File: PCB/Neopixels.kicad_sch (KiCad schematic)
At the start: 47 parts

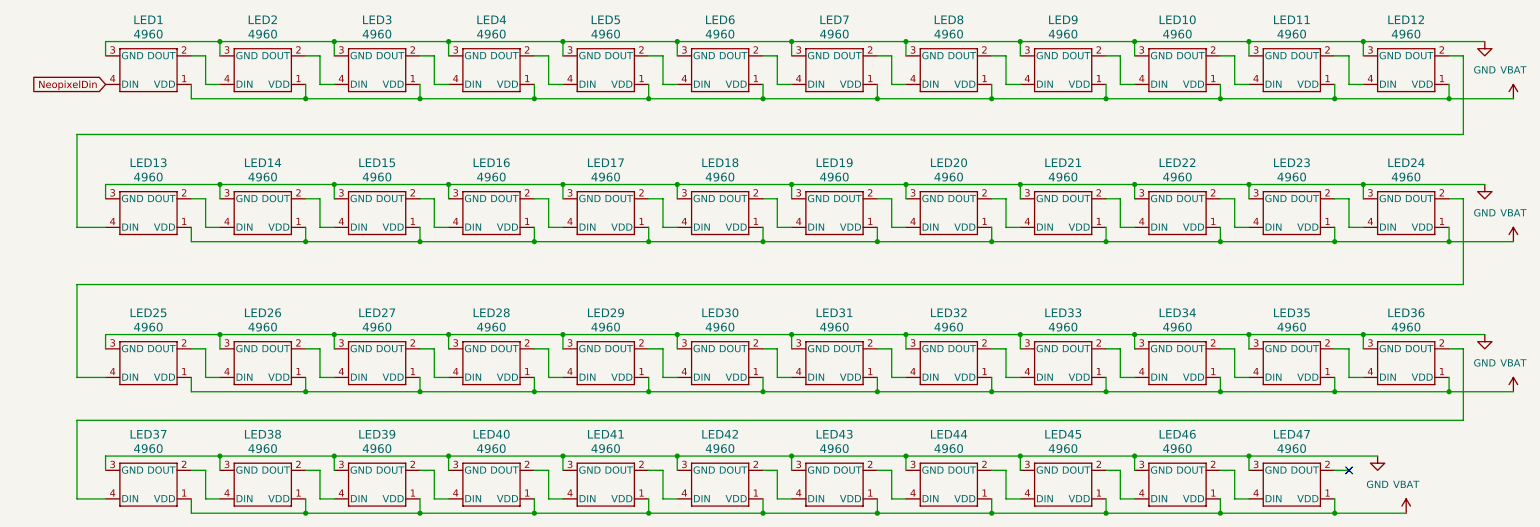
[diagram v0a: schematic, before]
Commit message: reorg symbols to be locally stored
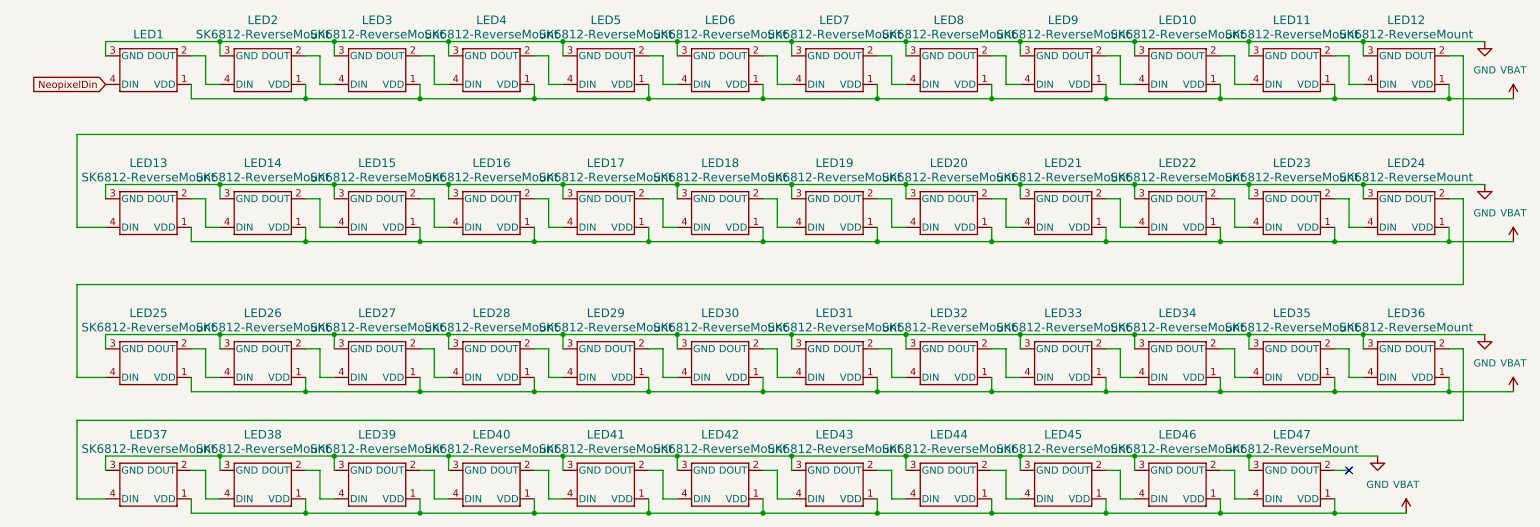
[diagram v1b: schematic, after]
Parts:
- LED1, LED10, LED11, LED12, LED13, LED14, LED15, LED16, LED17, LED18, LED19, LED2, LED20, LED21, LED22, LED23, LED24, LED25, LED26, LED27, LED28, LED29, LED3, LED30, LED31, LED32, LED33, LED34, LED35, LED36, LED37, LED38, LED39, LED4, LED40, LED41, LED42, LED43, LED44, LED45, LED46, LED47, LED5, LED6, LED7, LED8, LED9: value 4960 -> SK6812-ReverseMount; footprint kbd:YS-SK6812MINI-E -> 4960_ADA; symbol SK6812 Reverse mount:4960 -> Local-lib:SK6812-ReverseMount

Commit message: update to use local footprints
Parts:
- LED1, LED10, LED11, LED12, LED13, LED14, LED15, LED16, LED17, LED18, LED19, LED2, LED20, LED21, LED22, LED23, LED24, LED25, LED26, LED27, LED28, LED29, LED3, LED30, LED31, LED32, LED33, LED34, LED35, LED36, LED37, LED38, LED39, LED4, LED40, LED41, LED42, LED43, LED44, LED45, LED46, LED47, LED5, LED6, LED7, LED8, LED9: footprint 4960_ADA -> Local-lib:YS-SK6812MINI-E
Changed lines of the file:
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@@
 			)
 		)
-		(property "Footprint" "4960_ADA"
+		(property "Footprint" "Local-lib:YS-SK6812MINI-E"
 			(at 76.2 82.55 0)
 			(hide yes)
@@
 			)
 		)
-		(property "Footprint" "4960_ADA"
+		(property "Footprint" "Local-lib:YS-SK6812MINI-E"
 			(at 55.88 55.88 0)
 			(hide yes)
@@
 			)
 		)
-		(property "Footprint" "4960_ADA"
+		(property "Footprint" "Local-lib:YS-SK6812MINI-E"
 			(at 177.8 55.88 0)
 			(hide yes)
@@
 			)
 		)
-		(property "Footprint" "4960_ADA"
+		(property "Footprint" "Local-lib:YS-SK6812MINI-E"
 			(at 116.84 104.14 0)
 			(hide yes)
@@
 			)
 		)
-		(property "Footprint" "4960_ADA"
+		(property "Footprint" "Local-lib:YS-SK6812MINI-E"
 			(at 177.8 30.48 0)
 			(hide yes)
@@
 			)
 		)
-		(property "Footprint" "4960_ADA"
+		(property "Footprint" "Local-lib:YS-SK6812MINI-E"
 			(at 157.48 30.48 0)
 			(hide yes)
@@
 			)
 		)
-		(property "Footprint" "4960_ADA"
+		(property "Footprint" "Local-lib:YS-SK6812MINI-E"
 			(at 177.8 104.14 0)
 			(hide yes)
@@
 			)
 		)
-		(property "Footprint" "4960_ADA"
+		(property "Footprint" "Local-lib:YS-SK6812MINI-E"
 			(at 137.16 82.55 0)
 			(hide yes)
@@
 			)
 		)
-		(property "Footprint" "4960_ADA"
+		(property "Footprint" "Local-lib:YS-SK6812MINI-E"
 			(at 96.52 82.55 0)
 			(hide yes)
@@
 			)
 		)
-		(property "Footprint" "4960_ADA"
+		(property "Footprint" "Local-lib:YS-SK6812MINI-E"
 			(at 137.16 30.48 0)
 			(hide yes)
@@
 			)
 		)
-		(property "Footprint" "4960_ADA"
+		(property "Footprint" "Local-lib:YS-SK6812MINI-E"
 			(at 259.08 30.48 0)
 			(hide yes)
@@
 			)
 		)
-		(property "Footprint" "4960_ADA"
+		(property "Footprint" "Local-lib:YS-SK6812MINI-E"
 			(at 35.56 82.55 0)
 			(hide yes)
@@
 			)
 		)
-		(property "Footprint" "4960_ADA"
+		(property "Footprint" "Local-lib:YS-SK6812MINI-E"
 			(at 137.16 104.14 0)
 			(hide yes)
@@
 			)
 		)
-		(property "Footprint" "4960_ADA"
+		(property "Footprint" "Local-lib:YS-SK6812MINI-E"
 			(at 198.12 55.88 0)
 			(hide yes)
@@
 			)
 		)
-		(property "Footprint" "4960_ADA"
+		(property "Footprint" "Local-lib:YS-SK6812MINI-E"
 			(at 218.44 30.48 0)
 			(hide yes)
@@
 			)
 		)
-		(property "Footprint" "4960_ADA"
+		(property "Footprint" "Local-lib:YS-SK6812MINI-E"
 			(at 116.84 30.48 0)
 			(hide yes)
@@
 			)
 		)
-		(property "Footprint" "4960_ADA"
+		(property "Footprint" "Local-lib:YS-SK6812MINI-E"
 			(at 157.48 55.88 0)
 			(hide yes)
@@
 			)
 		)
-		(property "Footprint" "4960_ADA"
+		(property "Footprint" "Local-lib:YS-SK6812MINI-E"
 			(at 177.8 82.55 0)
 			(hide yes)
@@
 			)
 		)
-		(property "Footprint" "4960_ADA"
+		(property "Footprint" "Local-lib:YS-SK6812MINI-E"
 			(at 76.2 30.48 0)
 			(hide yes)
@@
 			)
 		)
-		(property "Footprint" "4960_ADA"
+		(property "Footprint" "Local-lib:YS-SK6812MINI-E"
 			(at 35.56 104.14 0)
 			(hide yes)
@@
 			)
 		)
-		(property "Footprint" "4960_ADA"
+		(property "Footprint" "Local-lib:YS-SK6812MINI-E"
 			(at 55.88 104.14 0)
 			(hide yes)
@@
 			)
 		)
-		(property "Footprint" "4960_ADA"
+		(property "Footprint" "Local-lib:YS-SK6812MINI-E"
 			(at 116.84 82.55 0)
 			(hide yes)
@@
 			)
 		)
-		(property "Footprint" "4960_ADA"
+		(property "Footprint" "Local-lib:YS-SK6812MINI-E"
 			(at 198.12 30.48 0)
 			(hide yes)
@@
 			)
 		)
-		(property "Footprint" "4960_ADA"
+		(property "Footprint" "Local-lib:YS-SK6812MINI-E"
 			(at 198.12 104.14 0)
 			(hide yes)
@@
 			)
 		)
-		(property "Footprint" "4960_ADA"
+		(property "Footprint" "Local-lib:YS-SK6812MINI-E"
 			(at 35.56 30.48 0)
 			(hide yes)
@@
 			)
 		)
-		(property "Footprint" "4960_ADA"
+		(property "Footprint" "Local-lib:YS-SK6812MINI-E"
 			(at 96.52 55.88 0)
 			(hide yes)
@@
 			)
 		)
-		(property "Footprint" "4960_ADA"
+		(property "Footprint" "Local-lib:YS-SK6812MINI-E"
 			(at 55.88 30.48 0)
 			(hide yes)
@@
 			)
 		)
-		(property "Footprint" "4960_ADA"
+		(property "Footprint" "Local-lib:YS-SK6812MINI-E"
 			(at 76.2 55.88 0)
 			(hide yes)
@@
 			)
 		)
-		(property "Footprint" "4960_ADA"
+		(property "Footprint" "Local-lib:YS-SK6812MINI-E"
 			(at 55.88 82.55 0)
 			(hide yes)
@@
 			)
 		)
-		(property "Footprint" "4960_ADA"
+		(property "Footprint" "Local-lib:YS-SK6812MINI-E"
 			(at 35.56 55.88 0)
 			(hide yes)
@@
 			)
 		)
-		(property "Footprint" "4960_ADA"
+		(property "Footprint" "Local-lib:YS-SK6812MINI-E"
 			(at 218.44 104.14 0)
 			(hide yes)
@@
 			)
 		)
-		(property "Footprint" "4960_ADA"
+		(property "Footprint" "Local-lib:YS-SK6812MINI-E"
 			(at 259.08 82.55 0)
 			(hide yes)
@@
 			)
 		)
-		(property "Footprint" "4960_ADA"
+		(property "Footprint" "Local-lib:YS-SK6812MINI-E"
 			(at 137.16 55.88 0)
 			(hide yes)
@@
 			)
 		)
-		(property "Footprint" "4960_ADA"
+		(property "Footprint" "Local-lib:YS-SK6812MINI-E"
 			(at 218.44 82.55 0)
 			(hide yes)
@@
 			)
 		)
-		(property "Footprint" "4960_ADA"
+		(property "Footprint" "Local-lib:YS-SK6812MINI-E"
 			(at 218.44 55.88 0)
 			(hide yes)
@@
 			)
 		)
-		(property "Footprint" "4960_ADA"
+		(property "Footprint" "Local-lib:YS-SK6812MINI-E"
 			(at 238.76 104.14 0)
 			(hide yes)
@@
 			)
 		)
-		(property "Footprint" "4960_ADA"
+		(property "Footprint" "Local-lib:YS-SK6812MINI-E"
 			(at 96.52 104.14 0)
 			(hide yes)
@@
 			)
 		)
-		(property "Footprint" "4960_ADA"
+		(property "Footprint" "Local-lib:YS-SK6812MINI-E"
 			(at 259.08 55.88 0)
 			(hide yes)
@@
 			)
 		)
-		(property "Footprint" "4960_ADA"
+		(property "Footprint" "Local-lib:YS-SK6812MINI-E"
 			(at 116.84 55.88 0)
 			(hide yes)
@@
 			)
 		)
-		(property "Footprint" "4960_ADA"
+		(property "Footprint" "Local-lib:YS-SK6812MINI-E"
 			(at 238.76 30.48 0)
 			(hide yes)
@@
 			)
 		)
-		(property "Footprint" "4960_ADA"
+		(property "Footprint" "Local-lib:YS-SK6812MINI-E"
 			(at 76.2 104.14 0)
 			(hide yes)
@@
 			)
 		)
-		(property "Footprint" "4960_ADA"
+		(property "Footprint" "Local-lib:YS-SK6812MINI-E"
 			(at 157.48 104.14 0)
 			(hide yes)
@@
 			)
 		)
-		(property "Footprint" "4960_ADA"
+		(property "Footprint" "Local-lib:YS-SK6812MINI-E"
 			(at 198.12 82.55 0)
 			(hide yes)
@@
 			)
 		)
-		(property "Footprint" "4960_ADA"
+		(property "Footprint" "Local-lib:YS-SK6812MINI-E"
 			(at 157.48 82.55 0)
 			(hide yes)
@@
 			)
 		)
-		(property "Footprint" "4960_ADA"
+		(property "Footprint" "Local-lib:YS-SK6812MINI-E"
 			(at 238.76 82.55 0)
 			(hide yes)
@@
 			)
 		)
-		(property "Footprint" "4960_ADA"
+		(property "Footprint" "Local-lib:YS-SK6812MINI-E"
 			(at 96.52 30.48 0)
 			(hide yes)
@@
 			)
 		)
-		(property "Footprint" "4960_ADA"
+		(property "Footprint" "Local-lib:YS-SK6812MINI-E"
 			(at 238.76 55.88 0)
 			(hide yes)
